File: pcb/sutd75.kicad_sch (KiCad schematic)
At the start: 43 parts, among them J1 SWD Header, J2 UART header, J3 USB_C_Receptacle_USB2.0, J4 I2C header, SW1 BOOT0, SW2 BOOT1, SW3 RESET, U1 XC6206PxxxMR, U2 STM32F103RBTx, U3 USBLC6-2SC6

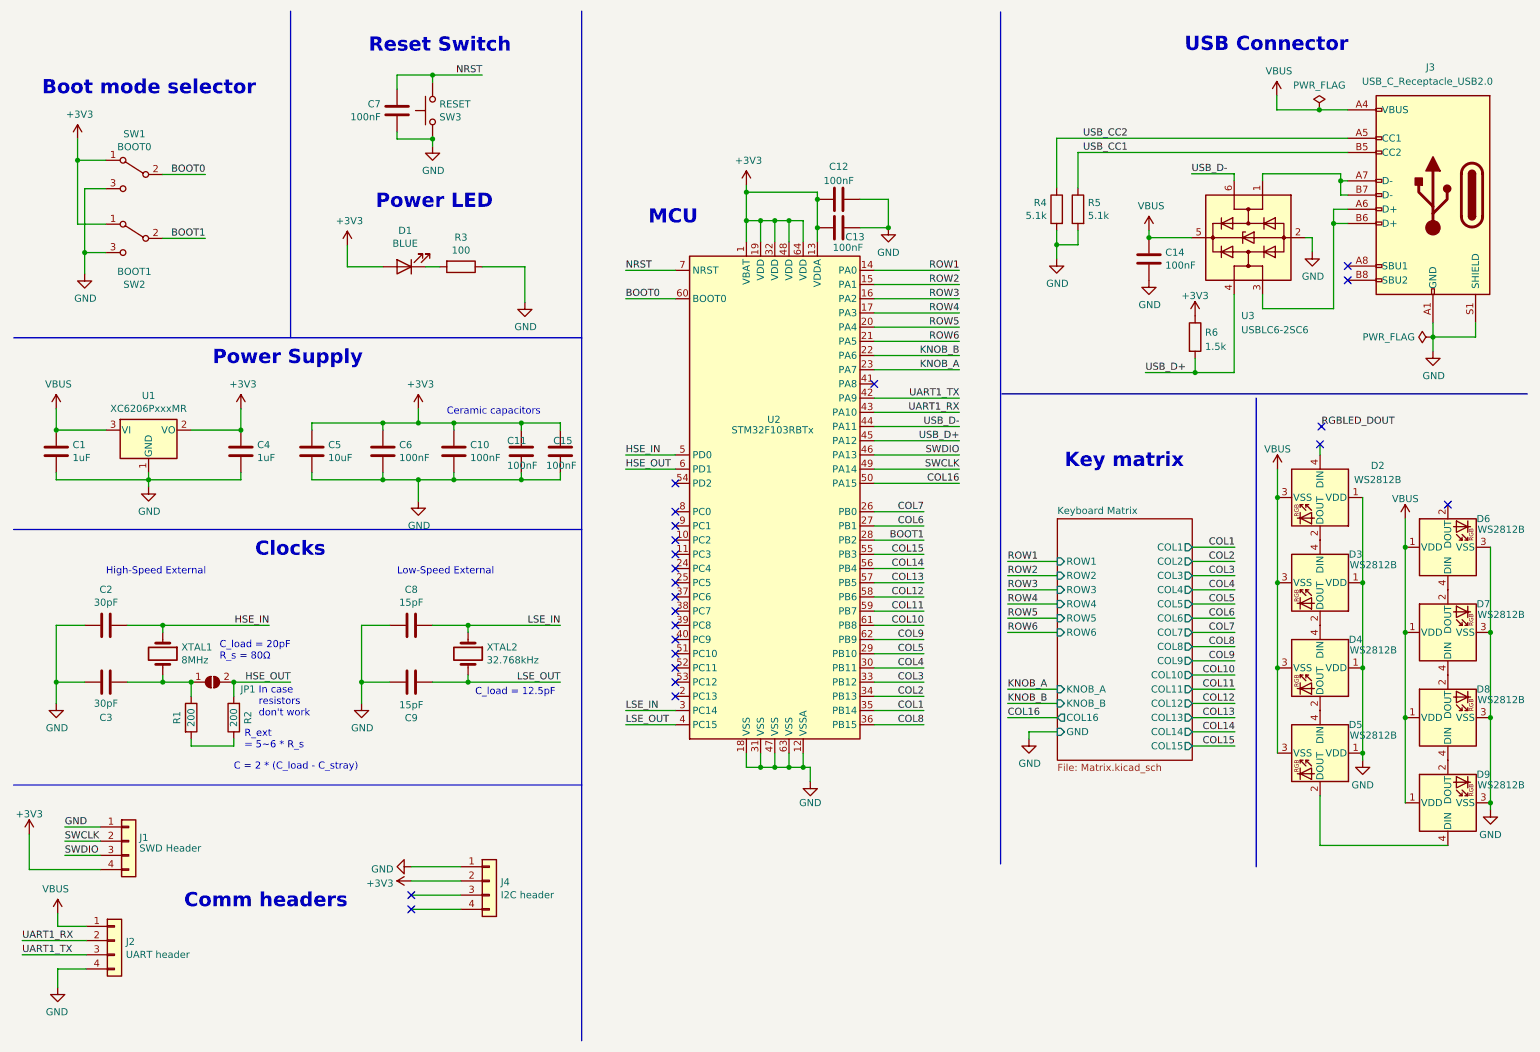
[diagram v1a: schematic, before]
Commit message: Add routing for rows and some of the columns
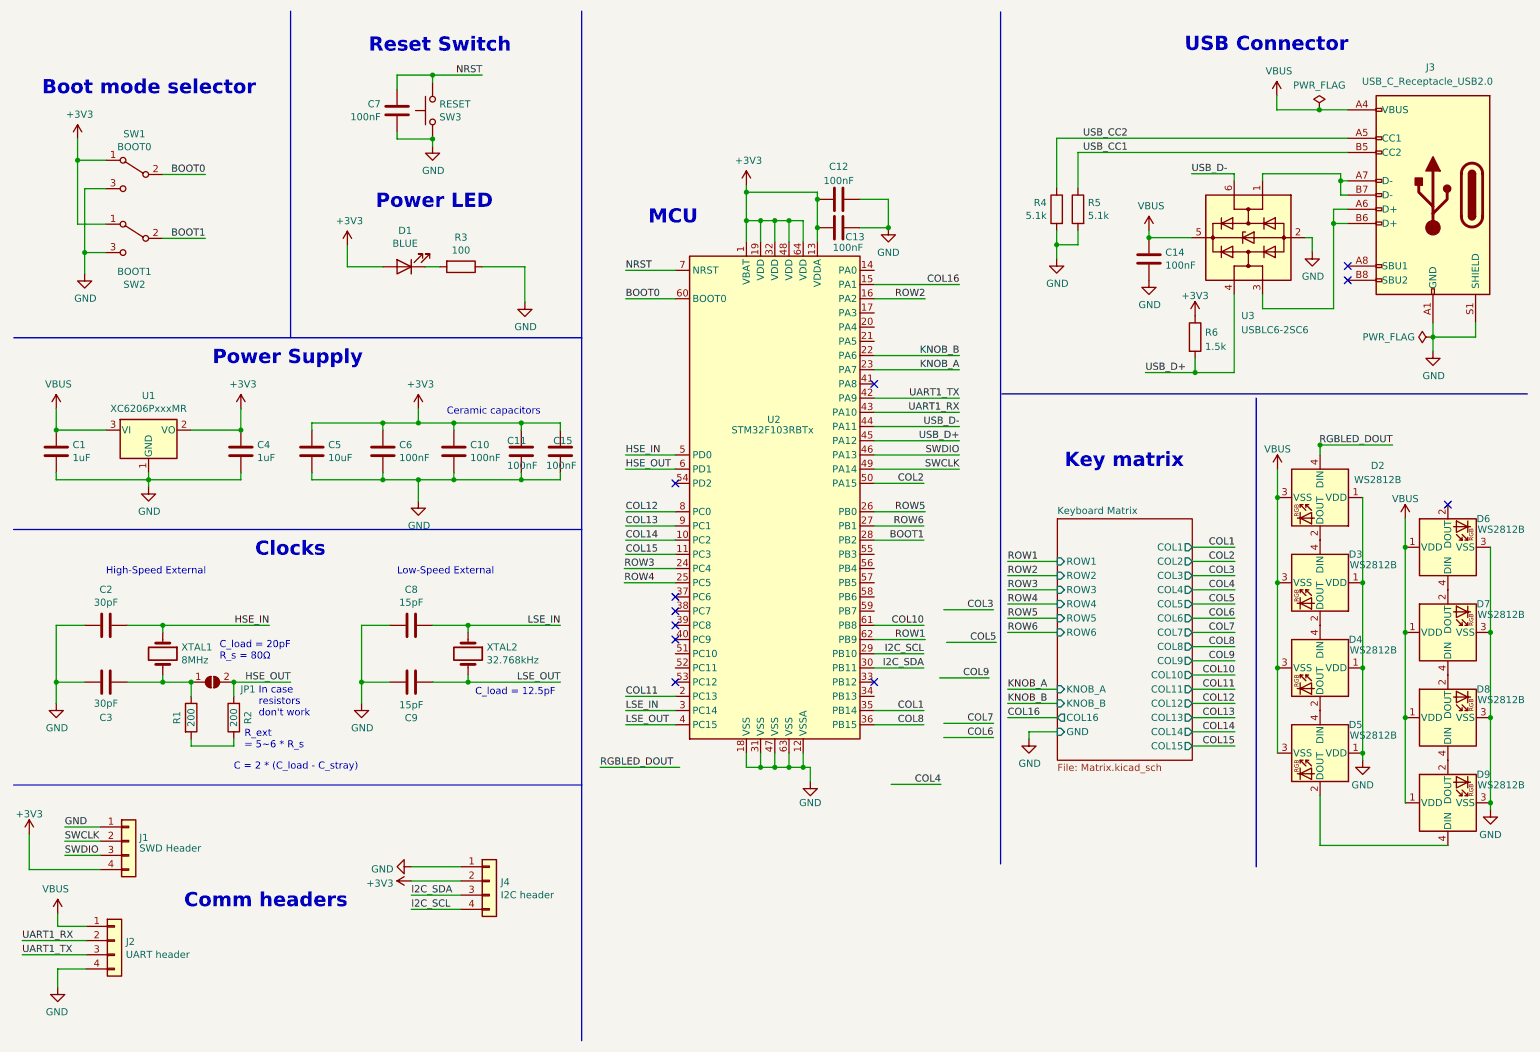
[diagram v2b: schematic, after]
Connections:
- net COL11: now also U2.2 (PC13); no longer U2.59 (PB7)
- net COL12: now also U2.8 (PC0); no longer U2.58 (PB6)
- net COL13: now also U2.9 (PC1); no longer U2.57 (PB5)
- net COL14: now also U2.10 (PC2); no longer U2.56 (PB4)
- net COL15: now also U2.11 (PC3); no longer U2.55 (PB3)
- net COL16: now also U2.15 (PA1); no longer U2.50 (PA15)
- net COL2: now also U2.50 (PA15); no longer U2.34 (PB13)
- net COL3: no longer U2.33 (PB12)
- net COL4: no longer U2.30 (PB11)
- net COL5: no longer U2.29 (PB10)
- net COL6: no longer U2.27 (PB1)
- net COL7: no longer U2.26 (PB0)
- net COL9: no longer U2.62 (PB9)
- net RGBLED_DOUT: now also D2.4 (DIN)
- net ROW1: now also U2.62 (PB9); no longer U2.14 (PA0)
- net ROW2: now also U2.16 (PA2); no longer U2.15 (PA1)
- net ROW3: now also U2.24 (PC4); no longer U2.16 (PA2)
- net ROW4: now also U2.25 (PC5); no longer U2.17 (PA3)
- net ROW5: now also U2.26 (PB0); no longer U2.20 (PA4)
- net ROW6: now also U2.27 (PB1); no longer U2.21 (PA5)
- net I2C_SDA: now reaches J4.3 (Pin_3)
- net I2C_SDA: now also U2.30 (PB11)
- net I2C_SCL: now reaches J4.4 (Pin_4)
- net I2C_SCL: now also U2.29 (PB10)
- no-connect marks 23 -> 11

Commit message: Wire up switch sockets to diodes
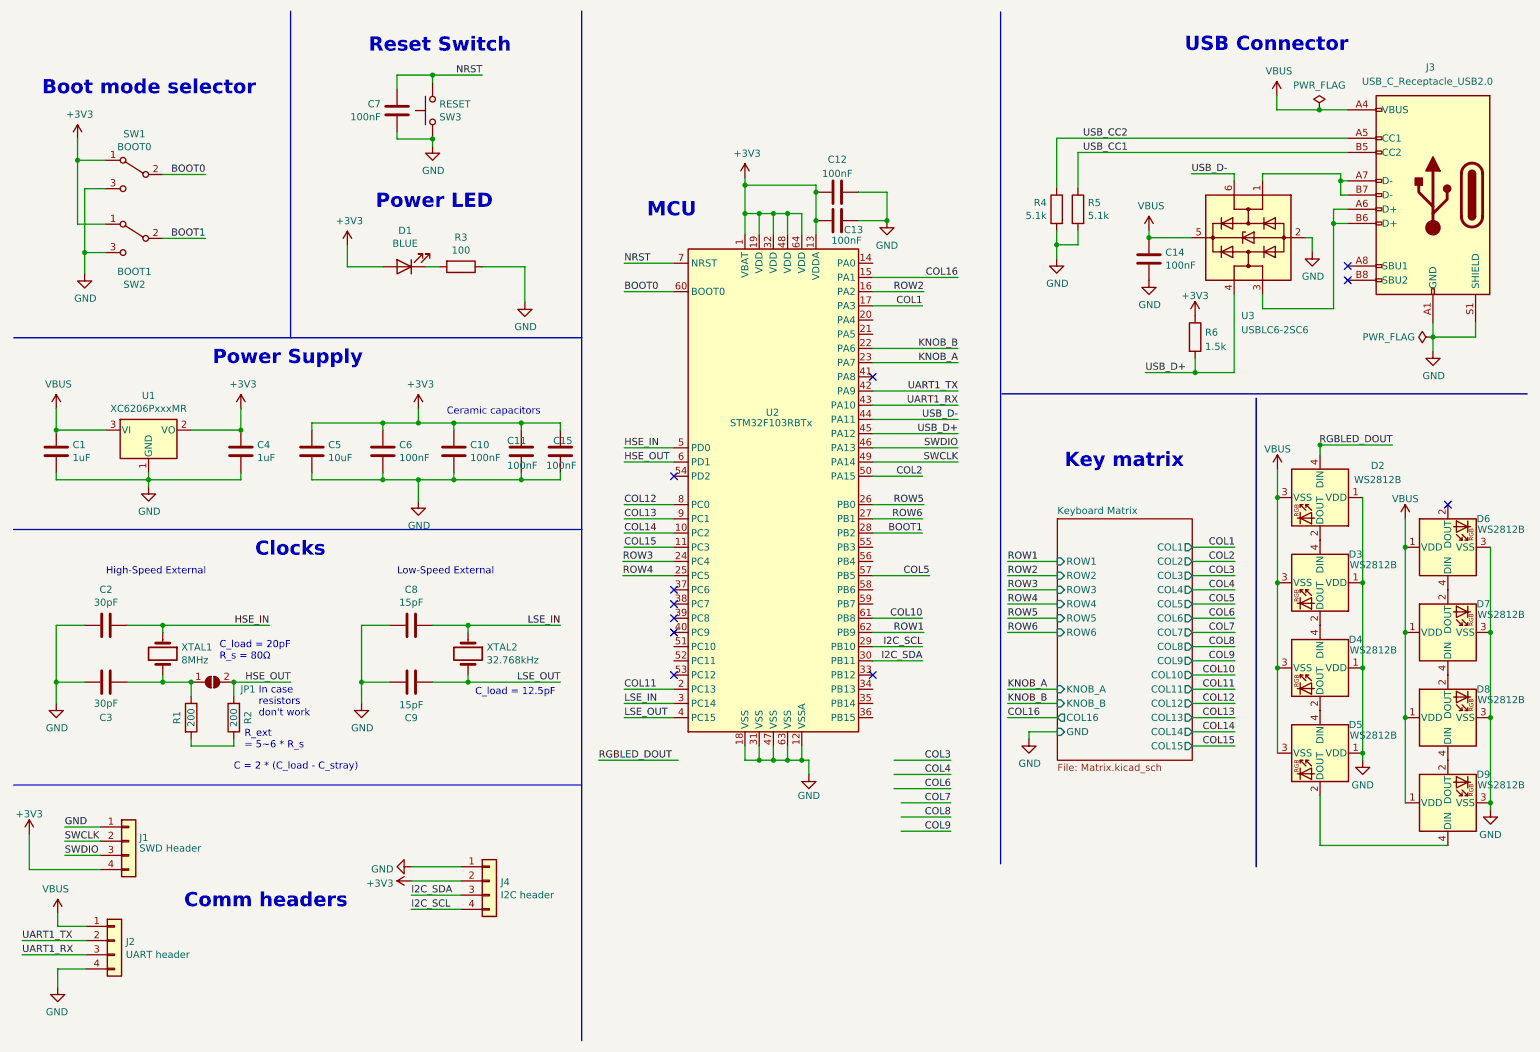
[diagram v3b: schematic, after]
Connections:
- net COL1: now also U2.17 (PA3); no longer U2.35 (PB14)
- net COL5: now also U2.57 (PB5)
- net COL8: no longer U2.36 (PB15)
- net UART1_RX: now also J2.3 (Pin_3); no longer J2.2 (Pin_2)
- net UART1_TX: now also J2.2 (Pin_2); no longer J2.3 (Pin_3)
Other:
- moved on the sheet: C12, C13, U2

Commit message: Move SWD header, fix DRC issues
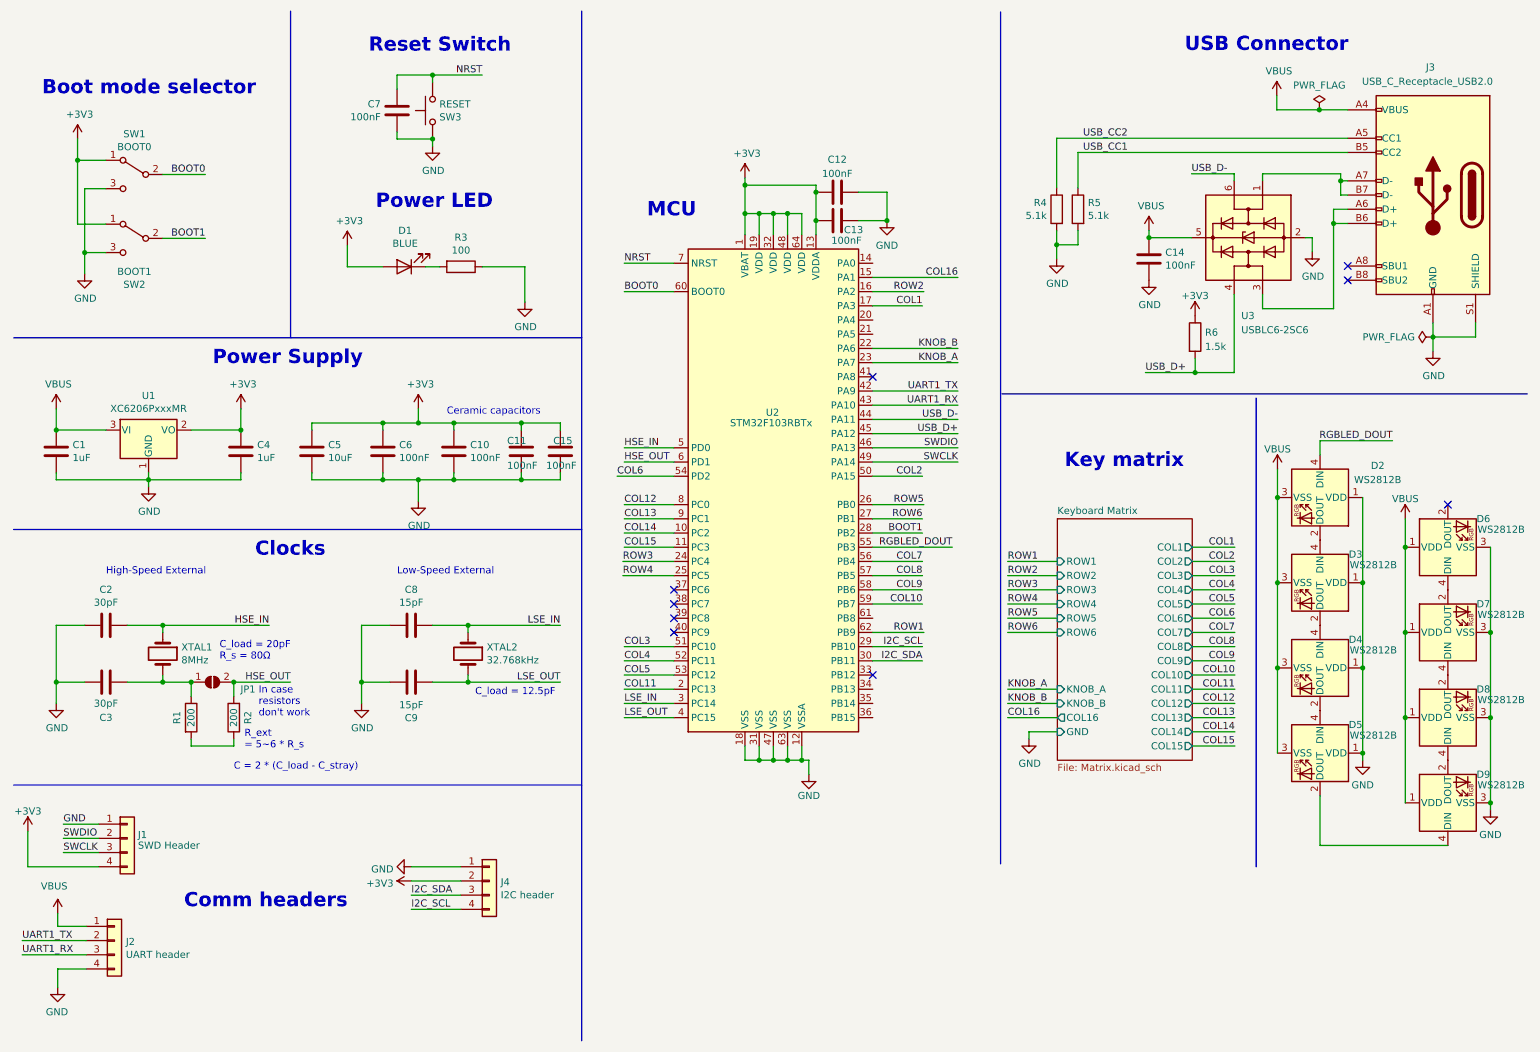
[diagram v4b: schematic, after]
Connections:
- net COL10: now also U2.59 (PB7); no longer U2.61 (PB8)
- net COL3: now also U2.51 (PC10)
- net COL4: now also U2.52 (PC11)
- net COL5: now also U2.53 (PC12); no longer U2.57 (PB5)
- net COL6: now also U2.54 (PD2)
- net COL7: now also U2.56 (PB4)
- net COL8: now also U2.57 (PB5)
- net COL9: now also U2.58 (PB6)
- net RGBLED_DOUT: now also U2.55 (PB3)
- net SWCLK: now also J1.3 (Pin_3); no longer J1.2 (Pin_2)
- net SWDIO: now also J1.2 (Pin_2); no longer J1.3 (Pin_3)
- no-connect marks 11 -> 9
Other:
- moved on the sheet: J1
